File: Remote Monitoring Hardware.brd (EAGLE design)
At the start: 74.9 x 52.7 mm, 39 parts, among them IC1 MSP430G2553, IC3 Xbee S3 Socket, IC4 MAX31855T, J5B PCC-SMP, Q1 32.768kHz

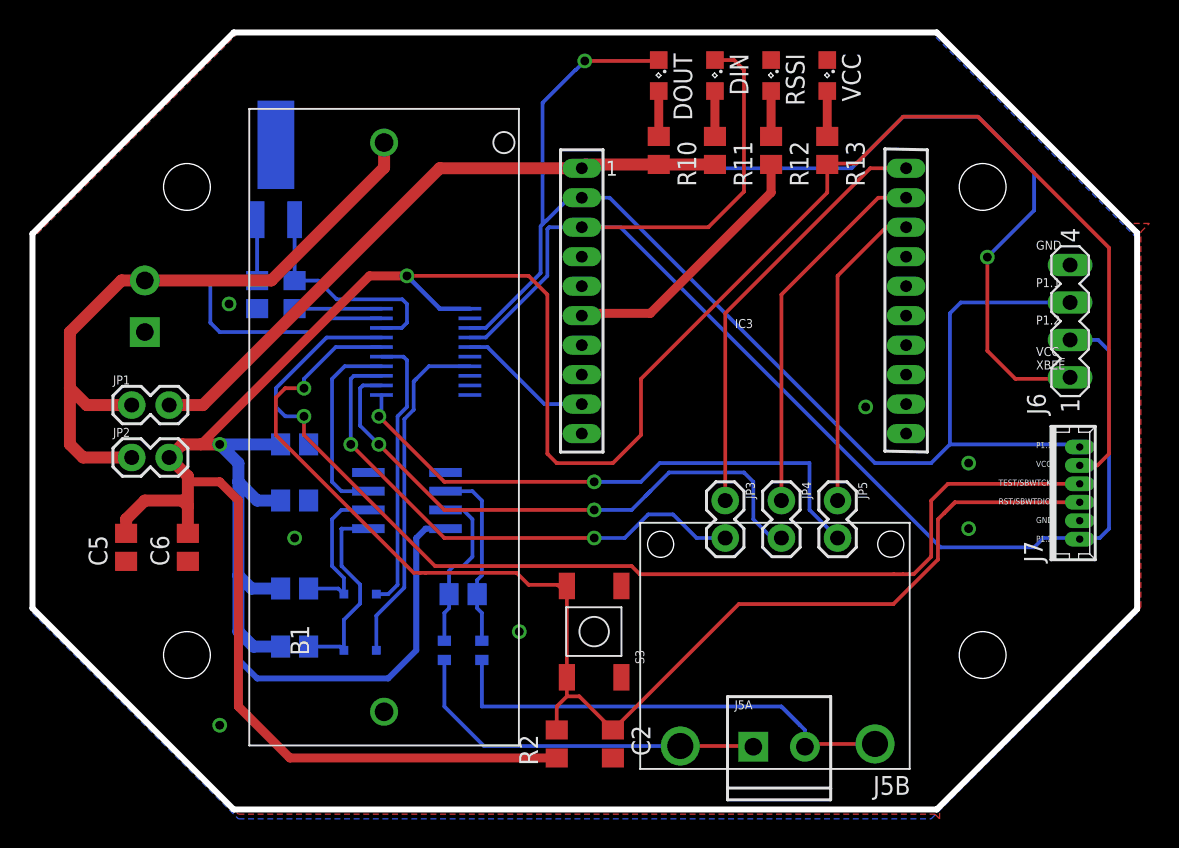
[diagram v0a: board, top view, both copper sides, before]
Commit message: larger msp430 programmer pins , new eagle project setup
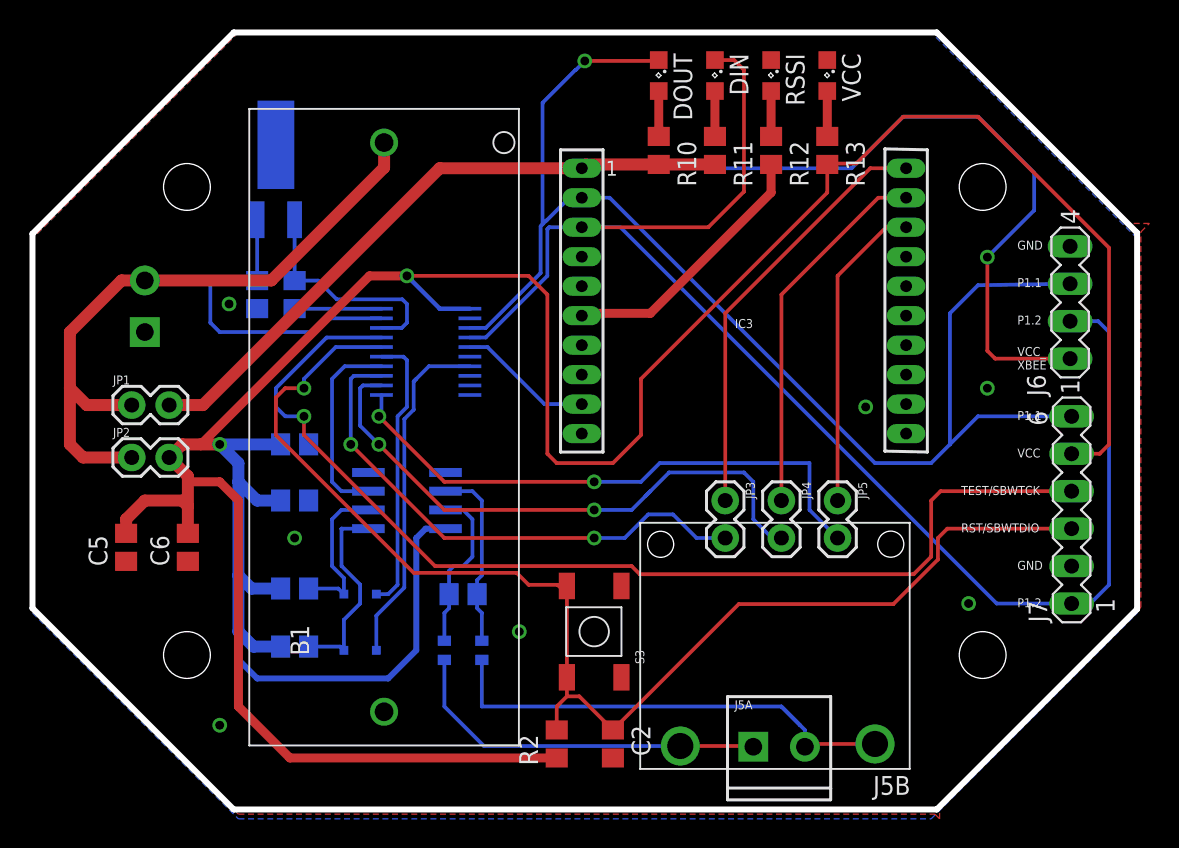
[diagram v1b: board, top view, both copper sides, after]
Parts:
- J7: device con-molex:53047-06 -> con-lstb:MA06-1
- moved J6 1.27 mm to (-4.55, 7.09)
- moved J7 1.15 mm to (-4.45, -6.99), turned to 90 degrees
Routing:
- net P1.2: track 95.5 -> 102.0 mm
- net RST/SBWTDIO: track 90.5 -> 87.4 mm
- net TEST/SBWTCK: track 74.6 -> 73.8 mm
- net VCC_XBEE: track 97.3 -> 96.7 mm
